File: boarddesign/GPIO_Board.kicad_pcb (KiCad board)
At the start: 2 copper layers, 86.4 x 77.5 mm, 63 parts, among them P1 ANA1, P10 I2C_PORT, P11 SPI_PORT, P12 ARM_PORT, P13 RASPBERRY PI GPIO CONN, P14 PROP PLUG, P15 RASPBERRY PI 40-PIN CONN, P16 DIO_PORTA_P1, P17 DIO_PORTA_P2, P18 DIO_PORTA_P3, P19 DIO_PORTA_P4, P2 ANA2, P20 DIO_PORTA_P5, P21 DIO_PORTA_P6, P22 DIO_PORTA_P7, P23 DIO_PORTA_P8, P24 USER COMM, P26 DIO_PORTB_P1, P27 DIO_PORTB_P2, P28 DIO_PORTB_P3, P29 DIO_PORTB_P4, P3 ANA3, P30 DIO_PORTB_P5, P31 DIO_PORTB_P6, P32 DIO_PORTB_P7, P33 DIO_PORTB_P8, P4 ANA4, P5 ANA5, P6 ANA6, P7 ANA7, P8 ANA8, P9 POWER_CONN, Q1 BSS138, U1 MCP3208, U2 P8X32A-D40, U3 24LC256, Y1 5 MHz

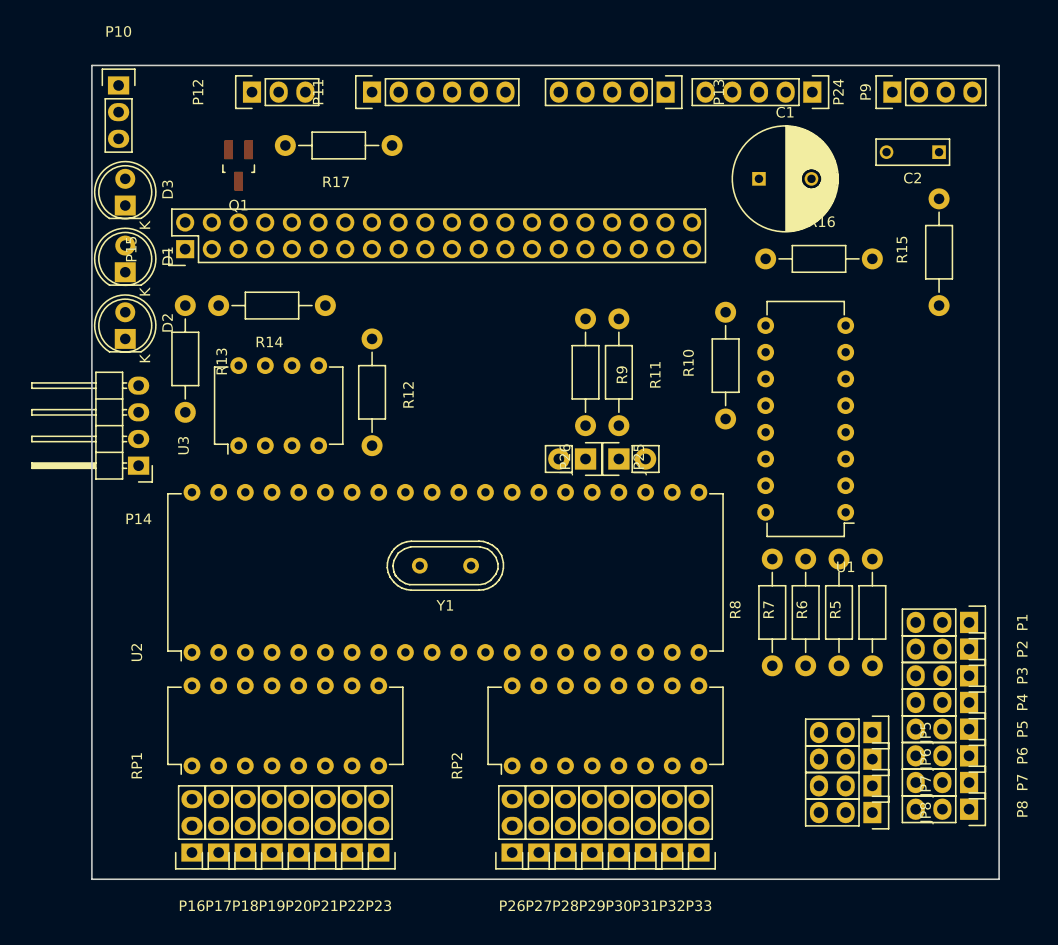
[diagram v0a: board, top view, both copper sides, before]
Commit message: Started routing board.
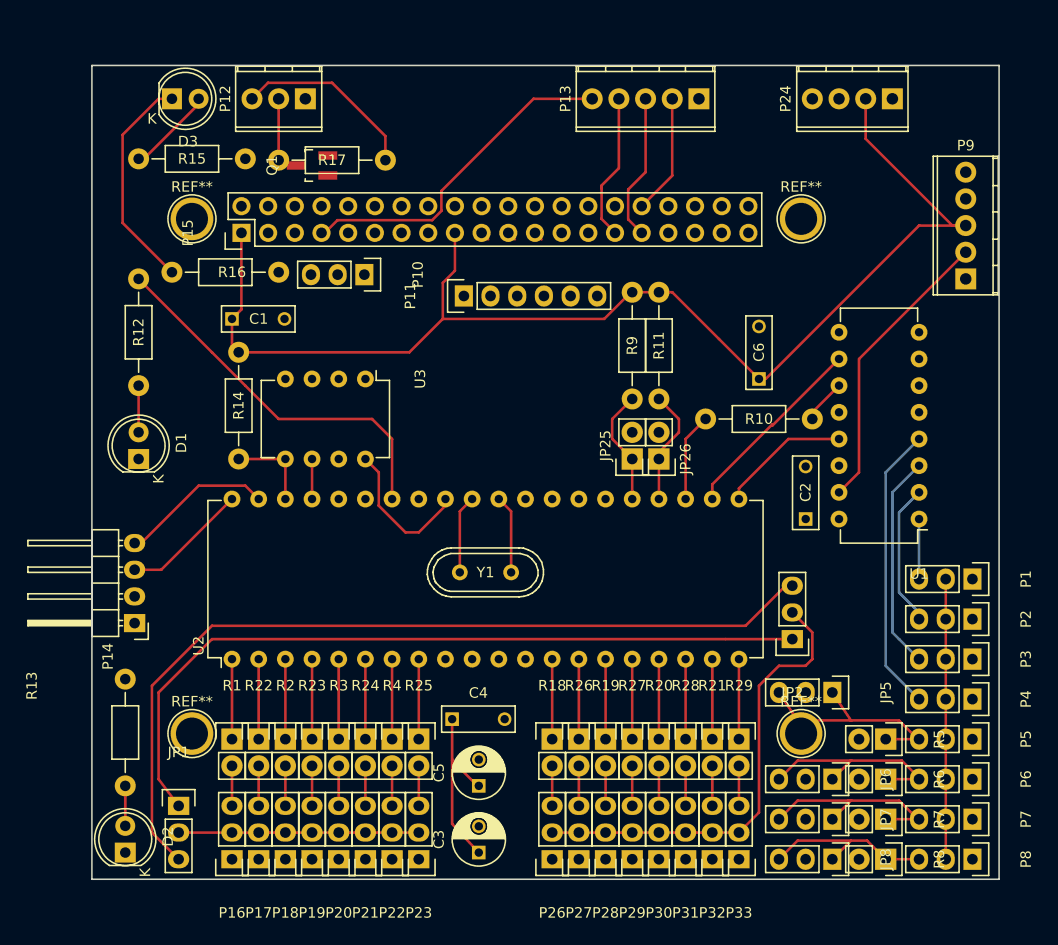
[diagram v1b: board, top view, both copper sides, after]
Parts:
- removed RP1, RP2: 8X 3.9 kOhm, Housings_DIP:DIP-16_W7.62mm
- added C3: 33 uF, Capacitors_ThroughHole:C_Radial_D5_L6_P2.5, F.Cu at (98.4, 123.8)
- added C4: 100 nF, Capacitors_ThroughHole:C_Rect_L7_W2.5_P5, F.Cu at (95.9, 111.1)
- added C5: 33 uF, Capacitors_ThroughHole:C_Radial_D5_L6_P2.5, F.Cu at (98.4, 117.5)
- added C6: 100 nF, Capacitors_ThroughHole:C_Rect_L7_W2.5_P5, F.Cu at (125.1, 78.7)
- added JP1: JUMPER3, Pin_Headers:Pin_Header_Straight_1x03, F.Cu at (69.8, 119.4)
- added JP2: JUMPER3, Pin_Headers:Pin_Header_Straight_1x03, F.Cu at (128.3, 103.5)
- added R1: 3.9 kOhm, Pin_Headers:Pin_Header_Straight_1x02, F.Cu at (74.9, 113.0)
- added R18: 3.9 kOhm, Pin_Headers:Pin_Header_Straight_1x02, F.Cu at (105.4, 113.0)
- added R19: 3.9 kOhm, Pin_Headers:Pin_Header_Straight_1x02, F.Cu at (110.5, 113.0)
- added R2: 3.9 kOhm, Pin_Headers:Pin_Header_Straight_1x02, F.Cu at (80.0, 113.0)
- added R20: 3.9 kOhm, Pin_Headers:Pin_Header_Straight_1x02, F.Cu at (115.6, 113.0)
- added R21: 3.9 kOhm, Pin_Headers:Pin_Header_Straight_1x02, F.Cu at (120.7, 113.0)
- added R22: 3.9 kOhm, Pin_Headers:Pin_Header_Straight_1x02, F.Cu at (77.5, 113.0)
- added R23: 3.9 kOhm, Pin_Headers:Pin_Header_Straight_1x02, F.Cu at (82.5, 113.0)
- added R24: 3.9 kOhm, Pin_Headers:Pin_Header_Straight_1x02, F.Cu at (87.6, 113.0)
- added R25: 3.9 kOhm, Pin_Headers:Pin_Header_Straight_1x02, F.Cu at (92.7, 113.0)
- added R26: 3.9 kOhm, Pin_Headers:Pin_Header_Straight_1x02, F.Cu at (108.0, 113.0)
- added R27: 3.9 kOhm, Pin_Headers:Pin_Header_Straight_1x02, F.Cu at (113.0, 113.0)
- added R28: 3.9 kOhm, Pin_Headers:Pin_Header_Straight_1x02, F.Cu at (118.1, 113.0)
- added R29: 3.9 kOhm, Pin_Headers:Pin_Header_Straight_1x02, F.Cu at (123.2, 113.0)
- added R3: 3.9 kOhm, Pin_Headers:Pin_Header_Straight_1x02, F.Cu at (85.1, 113.0)
- added R4: 3.9 kOhm, Pin_Headers:Pin_Header_Straight_1x02, F.Cu at (90.2, 113.0)
- added REF**: 1pin, Connect:1pin, F.Cu at (129.1, 112.5)
- added REF**: 1pin, Connect:1pin, F.Cu at (71.1, 112.5)
- added REF**: 1pin, Connect:1pin, F.Cu at (71.1, 63.5)
- added REF**: 1pin, Connect:1pin, F.Cu at (129.1, 63.5)
- C1: value 100 uF -> 100 nF; footprint Capacitors_ThroughHole:C_Radial_D10_L21_P5 -> Capacitors_ThroughHole:C_Rect_L7_W2.5_P5
- C2: value .1 uF -> 100 nF
- P12: footprint Pin_Headers:Pin_Header_Straight_1x03 -> Terminal_Blocks:TerminalBlock_Pheonix_MPT-2.54mm_3pol
- P13: value RASPBERRY PI GPIO CONN -> PI GPIO CONN; footprint Pin_Headers:Pin_Header_Straight_1x05 -> Terminal_Blocks:TerminalBlock_Pheonix_MPT-2.54mm_5pol
- P24: footprint Pin_Headers:Pin_Header_Straight_1x04 -> Terminal_Blocks:TerminalBlock_Pheonix_MPT-2.54mm_4pol
- P9: footprint Pin_Headers:Pin_Header_Straight_1x05 -> Terminal_Blocks:TerminalBlock_Pheonix_MPT-2.54mm_5pol
- R5, R6, R7, R8: footprint Resistors_ThroughHole:Resistor_Horizontal_RM10mm -> Pin_Headers:Pin_Header_Straight_1x02
- moved R15 77.5 mm to (66.0, 57.8), turned to 0 degrees
- moved C1 51.9 mm to (74.9, 73.0)
- moved D2 48.9 mm to (64.8, 123.8)
- moved R16 46.4 mm to (79.4, 68.6), turned to 180 degrees
- moved R13 46.1 mm to (64.8, 117.5), turned to 90 degrees
- moved C2 37.2 mm to (129.5, 92.1), turned to 90 degrees
- moved P10 29.5 mm to (87.5, 68.8), turned to 270 degrees
- moved P9 23.0 mm to (144.8, 69.2), turned to 90 degrees
- moved R12 22.7 mm to (66.0, 79.4), turned to 90 degrees
- moved R8 21.3 mm to (137.2, 124.5), turned to 270 degrees
- moved P11 21.3 mm to (97.0, 70.8)
- moved D1 17.8 mm to (66.0, 86.4)
- moved R7 16.5 mm to (137.2, 120.7), turned to 270 degrees
- moved P14 15.0 mm to (65.7, 102.0)
- moved U3 13.6 mm to (87.6, 78.7), turned to 270 degrees
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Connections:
- P1 pad 1: Net-(P1-Pad1) -> GNDREF
- P11 pad 2: SPI0_SCLK -> SPI0_MOSI
- P11 pad 3: SPI0_MOSI -> SPI0_MISO
- P11 pad 4: SPI0_MISO -> SPI0_SCLK
- P16 pad 2: +BATT -> Net-(JP1-Pad2)
- P17 pad 2: +BATT -> Net-(JP1-Pad2)
- P18 pad 2: +BATT -> Net-(JP1-Pad2)
- P19 pad 2: +BATT -> Net-(JP1-Pad2)
- P2 pad 1: Net-(P1-Pad1) -> GNDREF
- P20 pad 2: +BATT -> Net-(JP1-Pad2)
- P21 pad 2: +BATT -> Net-(JP1-Pad2)
- P22 pad 2: +BATT -> Net-(JP1-Pad2)
- P23 pad 2: +BATT -> Net-(JP1-Pad2)
- P26 pad 2: +BATT -> Net-(JP2-Pad2)
- P27 pad 2: +BATT -> Net-(JP2-Pad2)
- P28 pad 2: +BATT -> Net-(JP2-Pad2)
- P29 pad 2: +BATT -> Net-(JP2-Pad2)
- P3 pad 1: Net-(P1-Pad1) -> GNDREF
- P30 pad 2: +BATT -> Net-(JP2-Pad2)
- P31 pad 2: +BATT -> Net-(JP2-Pad2)
- P32 pad 2: +BATT -> Net-(JP2-Pad2)
- P33 pad 2: +BATT -> Net-(JP2-Pad2)
- P4 pad 1: Net-(P1-Pad1) -> GNDREF
- P5 pad 1: Net-(P1-Pad1) -> GNDREF
- P6 pad 1: Net-(P6-Pad1) -> GNDREF
- P7 pad 1: Net-(P7-Pad1) -> GNDREF
- P8 pad 1: Net-(P8-Pad1) -> GNDREF
- R5 pad 2: Net-(P1-Pad1) -> GNDREF
- R6 pad 2: Net-(P6-Pad1) -> GNDREF
- R7 pad 2: Net-(P7-Pad1) -> GNDREF
- R8 pad 2: Net-(P8-Pad1) -> GNDREF
- U2 pad 22: Net-(R10-Pad1) -> Net-(U1-Pad10)
- U2 pad 23: Net-(U1-Pad10) -> Net-(R10-Pad1)
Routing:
- net +3V3: track 0.00 -> 176.4 mm
- net +5V: track 0.00 -> 82.5 mm
- net +BATT: track 0.00 -> 73.9 mm
- net Net-(JP2-Pad2): track 0.00 -> 43.9 mm
- net Net-(R12-Pad2): track 0.00 -> 36.2 mm
- net GPIO4: track 0.00 -> 32.2 mm
- net VAA: track 0.00 -> 27.9 mm
- net Net-(P4-Pad3): track 0.00 -> 27.4 mm
- net Net-(JP1-Pad2): track 0.00 -> 22.9 mm
- net Net-(JP5-Pad1): track 0.00 -> 21.9 mm
- net Net-(D3-Pad1): track 0.00 -> 21.1 mm
- net Net-(JP6-Pad1): track 0.00 -> 20.6 mm
- net Net-(P3-Pad3): track 0.00 -> 20.5 mm
- net Net-(JP7-Pad1): track 0.00 -> 20.4 mm
- net Net-(U1-Pad10): track 0.00 -> 18.6 mm
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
